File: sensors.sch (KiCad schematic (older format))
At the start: 75 parts, among them SW1 MicroSwitch, SW10 MicroSwitch, SW11 MicroSwitch, SW12 MicroSwitch, SW13 MicroSwitch, SW14 MicroSwitch, SW15 MicroSwitch, SW16 MicroSwitch, SW2 MicroSwitch, SW3 MicroSwitch, SW4 MicroSwitch, SW5 MicroSwitch, SW6 MicroSwitch, SW7 MicroSwitch, SW8 MicroSwitch, SW9 MicroSwitch, U5 BQ32000, X2 32768Hz

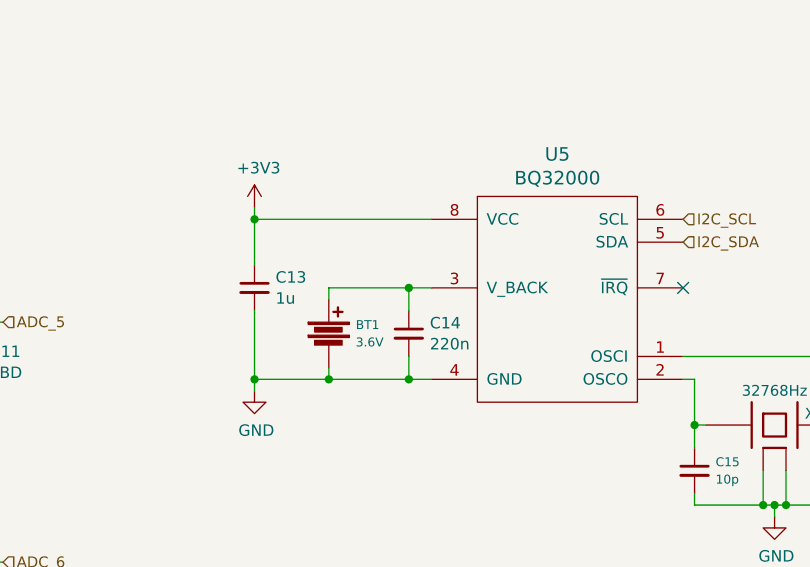
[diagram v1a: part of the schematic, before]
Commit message: Add a recharge circuit for the RTC backup battery
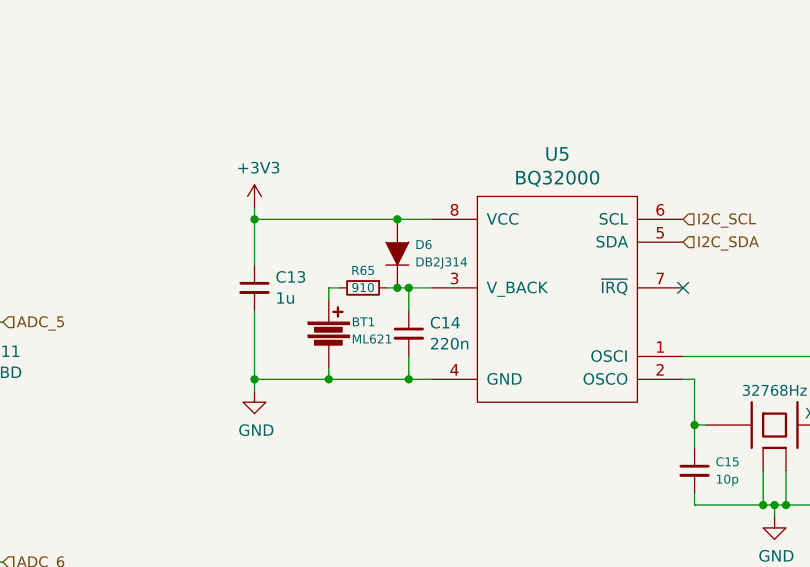
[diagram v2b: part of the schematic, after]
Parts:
- added D6: DB2J314, symbol D
- added R65: 910, symbol R_Small
- BT1: value 3.6V -> ML621
- C10, C11, C12, C13, C14, C15, C16, C7, C8, C9: footprint (none) -> _std:_0603
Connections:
- net +3V3: now also D6.2 (A)
- net at C14.1, U5.3 (V_BACK): now also D6.1 (K), R65.1; no longer BT1.1
- new net: BT1.1, R65.2

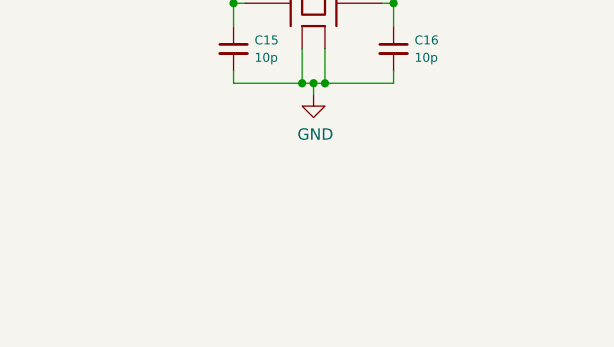
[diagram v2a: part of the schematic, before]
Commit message: Add CVRA logo to schematic
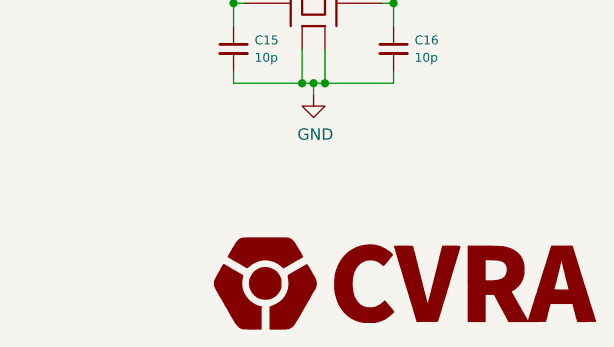
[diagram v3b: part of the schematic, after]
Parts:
- BT1: footprint (none) -> _div:Battery_ML621
- CONN10, CONN11, CONN12, CONN7, CONN8, CONN9, SW1, SW10, SW11, SW12, SW13, SW14, SW15, SW16, SW2, SW3, SW4, SW5, SW6, SW7, SW8, SW9: footprint (none) -> Pin_Headers:Pin_Header_Straight_1x02
- CONN13, CONN14, CONN15, CONN16: footprint (none) -> Pin_Headers:Pin_Header_Straight_1x03
- R11, R12, R13, R14, R15, R16, R17, R18, R19, R20, R21, R22, R23, R24, R25, R26, R27, R28, R29, R30, R31, R32, R33, R34, R35, R36, R37, R38, R39, R40, R41, R42, R65: footprint (none) -> _std:_0603

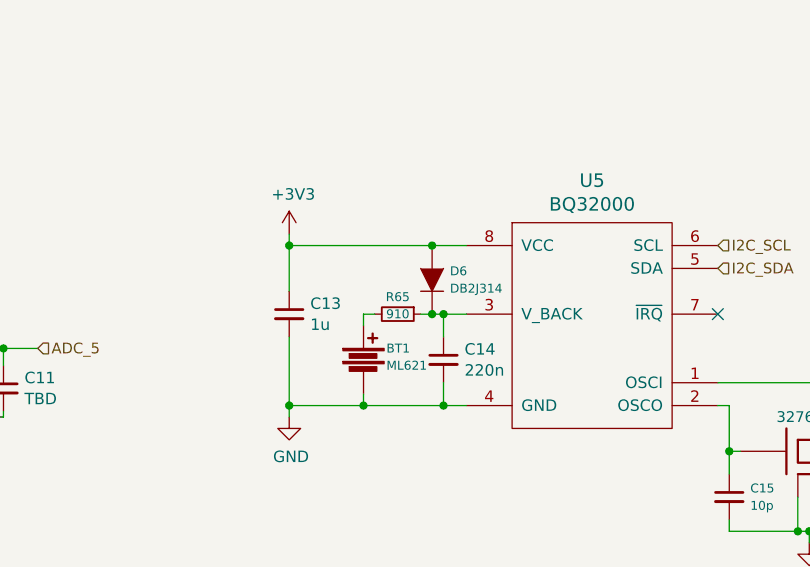
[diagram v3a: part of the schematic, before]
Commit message: Associate footprints
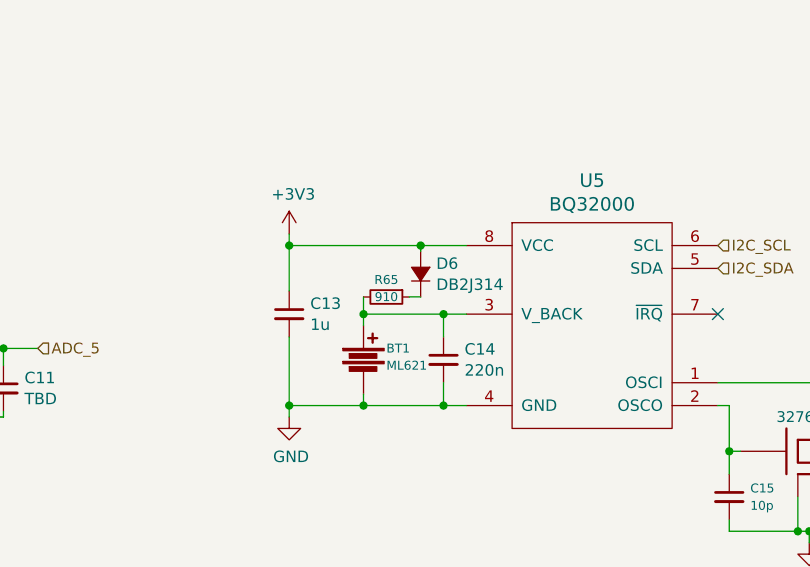
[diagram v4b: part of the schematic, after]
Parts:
- removed D6: DB2J314, symbol D
- added D6: DB2J314, _std:Diode_SMini2, symbol D_Small
- CONN10, CONN11, CONN12, CONN7, CONN8, CONN9, SW1, SW10, SW11, SW12, SW13, SW14, SW15, SW16, SW2, SW3, SW4, SW5, SW6, SW7, SW8, SW9: footprint Pin_Headers:Pin_Header_Straight_1x02 -> _connectors:_Pin2mm_2
- CONN13, CONN14, CONN15, CONN16: footprint Pin_Headers:Pin_Header_Straight_1x03 -> _connectors:_Pin2mm_3
- D2, D3, D4, D5: footprint (none) -> _std:_0603
- U5: footprint (none) -> _std:_SO-8
- X2: footprint (none) -> _div:XTAL_ABS07
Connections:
- net +3V3: now also D6.2 (A)
- net at C14.1, U5.3 (V_BACK): now also BT1.1, R65.2; no longer R65.1
- new net: D6.1 (K), R65.1
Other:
- moved on the sheet: R65

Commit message: Place components on PCB
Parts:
- removed X2: 32768Hz, _div:XTAL_ABS07, symbol XTAL-SMD-4-PADS
- added X2: 32768Hz, _div:XTAL_ABS07, symbol Crystal
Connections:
- net at C16.1, U5.1 (OSCI): now also X2.2
- net at C15.1, U5.2 (OSCO): now also X2.1
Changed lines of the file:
@@
 	9425 5300 10175 5300
 Wire Wire Line
-	9525 5600 9475 5600
+	9675 5600 9475 5600
 Wire Wire Line
 	9475 5400 9475 5700
@@
 	1    0    0    -1
 $EndComp
-$Comp
-L XTAL-SMD-4-PADS X2
-U 1 1 56B4F654
-P 9825 5600
-F 0 "X2" H 10000 5650 47  0000 C CNN
-F 1 "32768Hz" H 9825 5750 47  0000 C CNN
-F 2 "_div:XTAL_ABS07" H 9825 5600 60  0001 C CNN
-F 3 "" H 9825 5600 60  0000 C CNN
-	1    9825 5600
-	1    0    0    -1
-$EndComp
 Wire Wire Line
 	10175 5300 10175 5700
 Wire Wire Line
-	10175 5600 10125 5600
+	10175 5600 9975 5600
 Connection ~ 10175 5600
 Wire Wire Line
@@
 	10175 5950 10175 5900
 Connection ~ 9825 5950
-Wire Wire Line
-	9875 5950 9875 5800
-Connection ~ 9875 5950
-Wire Wire Line
-	9775 5800 9775 5950
-Connection ~ 9775 5950
 $Comp
 L C_Small C14
@@
 Connection ~ 7550 4700
 Connection ~ 8125 4700
+$Comp
+L Crystal X2
+U 1 1 56D345FF
+P 9825 5600
+F 0 "X2" H 9825 5450 50  0000 C CNN
+F 1 "32768Hz" H 9825 5750 50  0000 C CNN
+F 2 "_div:XTAL_ABS07" H 9825 5600 50  0001 C CNN
+F 3 "" H 9825 5600 50  0000 C CNN
+	1    9825 5600
+	1    0    0    -1
+$EndComp
 $EndSCHEMATC
